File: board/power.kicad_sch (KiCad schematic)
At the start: 10 parts, among them U2 OKI

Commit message: Fan, Light, Buck
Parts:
- removed R1: 1.5k, Resistor_SMD:R_0603_1608Metric_Pad0.98x0.95mm_HandSolder, symbol Device:R
- removed R2: 100, Resistor_SMD:R_0603_1608Metric_Pad0.98x0.95mm_HandSolder, symbol Device:R
- removed R3: 220, Resistor_SMD:R_0603_1608Metric_Pad0.98x0.95mm_HandSolder, symbol Device:R
- removed U2: OKI, MRDT_Devices:OKI_Horizontal, symbol MRDT_Devices:OKI
- added D19: Green, LED_SMD:LED_0603_1608Metric_Pad1.05x0.95mm_HandSolder, symbol Device:LED
- added R1: 820, symbol Device:R_US
- added R2: 6.8k, symbol Device:R_US
- added R23: 3k, symbol Device:R_US
- added R3: 330, symbol Device:R_US
- added U2: OKI-78SR-12_1.0-W36H-C, Converter_DCDC:Converter_DCDC_Murata_OKI-78SR_Horizontal, symbol Converter_DCDC:OKI-78SR-12_1.0-W36H-C
- added U3: SHHD003A0A, MRDT_Devices:SHHD003A0A41Z_Through_Hole, symbol MRDT_Devices:SHHD003A0A
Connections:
- net +3.3V: now also R3.1
- net +5V: now also R1.1, U3.6 (Vout+); no longer C2.1
- net GND: now also D19.1 (K), U2.2 (GND), U3.2 (Vin-), U3.3 (On/OFF), U3.4 (Vout-)
- net VCC: now also R2.1, U2.1 (IN), U3.1 (Vin+)
- net at D1.2 (A): now also R2.2
- net at D2.2 (A): now also R3.2
- net at D3.2 (A): now also R1.2
- new net: D19.2 (A), R23.2
- new net +12V: C2.1, R23.1, U2.3 (OUT)
- no-connect marks 0 -> 1
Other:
- moved on the sheet: D1, D2, D3

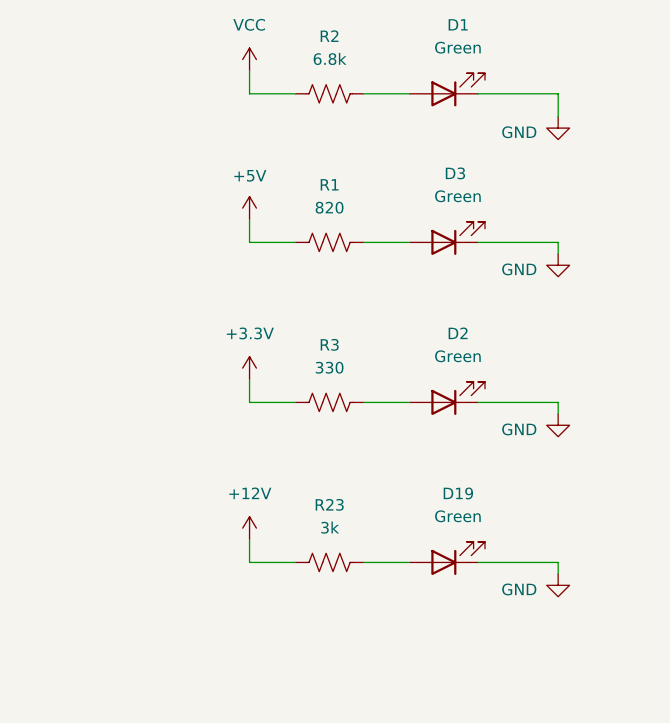
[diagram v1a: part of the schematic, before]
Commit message: Added most Footprints, Schematic review touch up
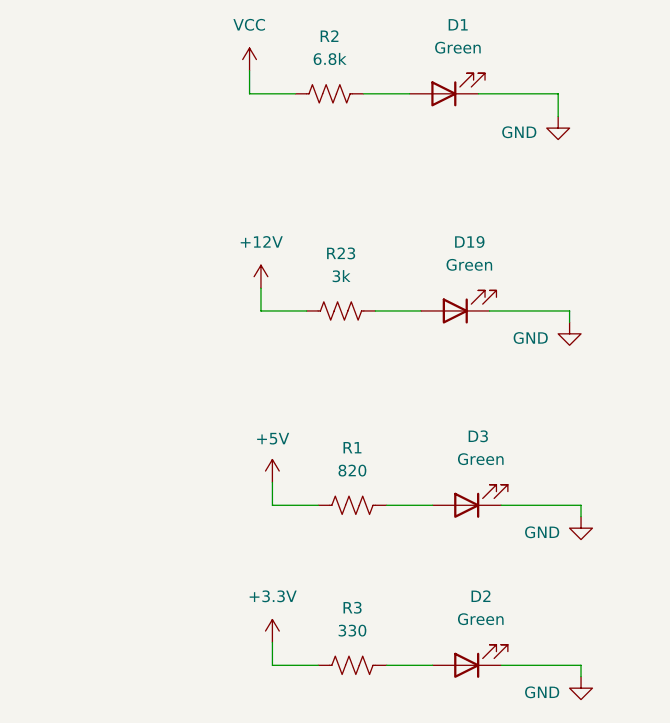
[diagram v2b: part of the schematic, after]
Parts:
- R1, R2, R23, R3: footprint (none) -> Resistor_SMD:R_0603_1608Metric_Pad0.98x0.95mm_HandSolder
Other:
- moved on the sheet: D19, D2, D3, R1, R23, R3

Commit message: Layout edits
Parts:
- removed Conn1: AndersonPP, MRDT_Connectors:Square_Anderson_2_H_Side_By_Side_PV, symbol MRDT_Connectors:AndersonPP
- added D20: MMSZ5240BT1G, MRDT_Devices:SOD-123_ONS-L, symbol MRDT_Devices:MMSZ5240BT1G
- added J2: 768250002, CoreBoard:CONN_SD-76825-0100_02_MOL, symbol CoreBoard:768250002
- added MOSFET1: TPC8132_LQS, MRDT_Devices:SOP-8_TOS-L, symbol MRDT_Devices:TPC8132_LQS
- added R10: 1k, Resistor_SMD:R_0603_1608Metric_Pad0.98x0.95mm_HandSolder, symbol Device:R_US
- U3: footprint MRDT_Devices:SHHD003A0A41Z_Through_Hole -> MRDT_Devices:SHHD003A0A-SRZ_Surface_Mount
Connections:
- net GND: now also D20.2, J2.1, R10.1
- new net: J2.2, MOSFET1.5 (DRAIN), MOSFET1.6 (DRAIN), MOSFET1.7 (DRAIN), MOSFET1.8 (DRAIN)
- new net: MOSFET1.4 (GATE), R10.2
- new net +24V: D20.1, MOSFET1.1 (SOURCE), MOSFET1.2 (SOURCE), MOSFET1.3 (SOURCE)

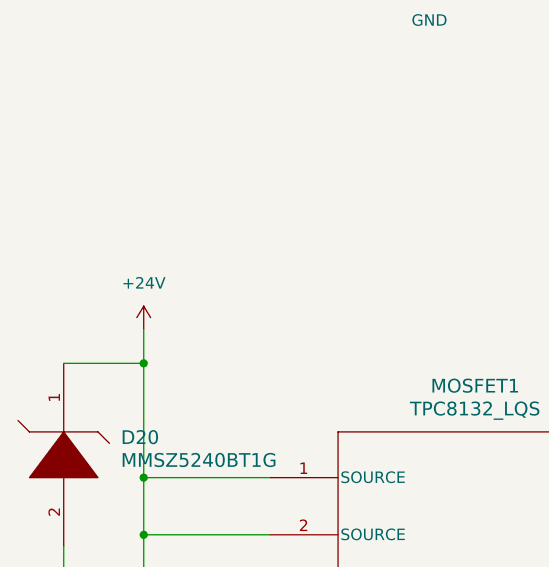
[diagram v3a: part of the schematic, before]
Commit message: routed core board
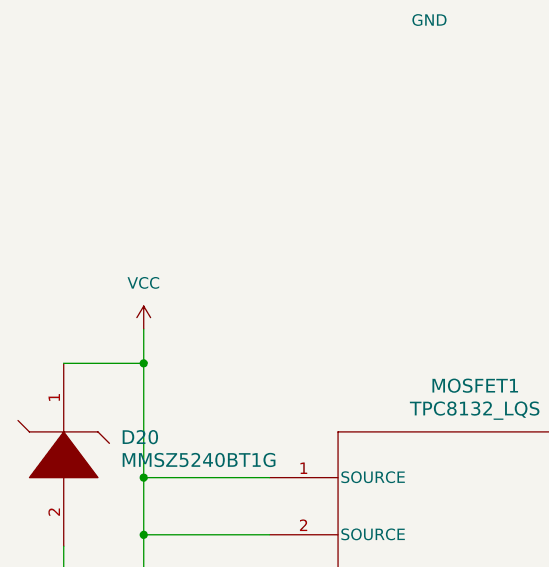
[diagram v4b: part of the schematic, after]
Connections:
- net +24V is gone; now on net VCC: D20.1, MOSFET1.1 (SOURCE), MOSFET1.2 (SOURCE), MOSFET1.3 (SOURCE)

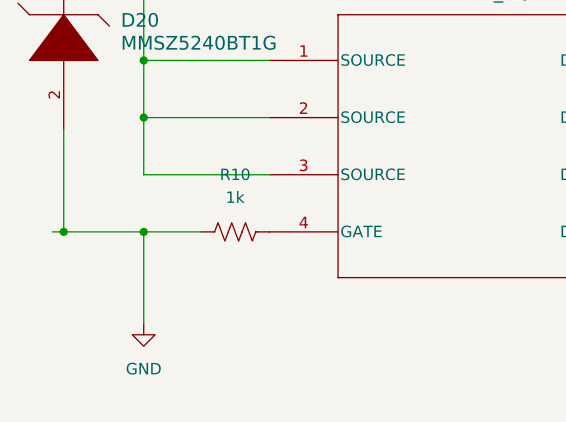
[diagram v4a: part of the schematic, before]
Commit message: Cleaned up traces and silkscreens
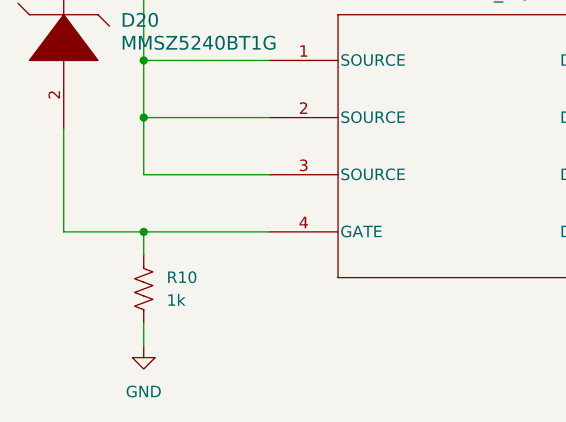
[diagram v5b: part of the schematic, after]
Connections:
- net GND: no longer D20.2
- net at MOSFET1.4 (GATE), R10.2: now also D20.2
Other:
- moved on the sheet: R10

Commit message: rev2 progress
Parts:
- removed U3: SHHD003A0A, MRDT_Devices:SHHD003A0A-SRZ_Surface_Mount, symbol MRDT_Devices:SHHD003A0A
- added C4: 10µF, Capacitor_SMD:C_1206_3216Metric_Pad1.33x1.80mm_HandSolder, symbol Device:C
- added C5: 10µF, Capacitor_SMD:C_0603_1608Metric_Pad1.08x0.95mm_HandSolder, symbol Device:C
- added U7: OKI-78SR-5_1.5-W36H-C, Converter_DCDC:Converter_DCDC_Murata_OKI-78SR_Horizontal, symbol Converter_DCDC:OKI-78SR-5_1.5-W36H-C
- MOSFET1: footprint MRDT_Devices:SOP-8_TOS-L -> CoreBoard:MSOP8_MC_MCH-L
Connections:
- net +12V: now also C5.1, U7.3 (OUT)
- net GND: now also C4.2, C5.2, U7.2 (GND)
- net VCC: now also C4.1, U7.1 (IN)
- no-connect marks 1 -> 0

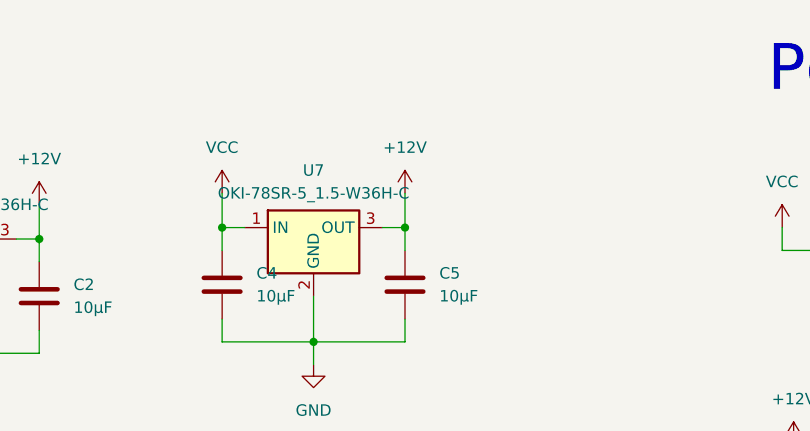
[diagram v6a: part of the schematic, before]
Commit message: move things for buck circuit
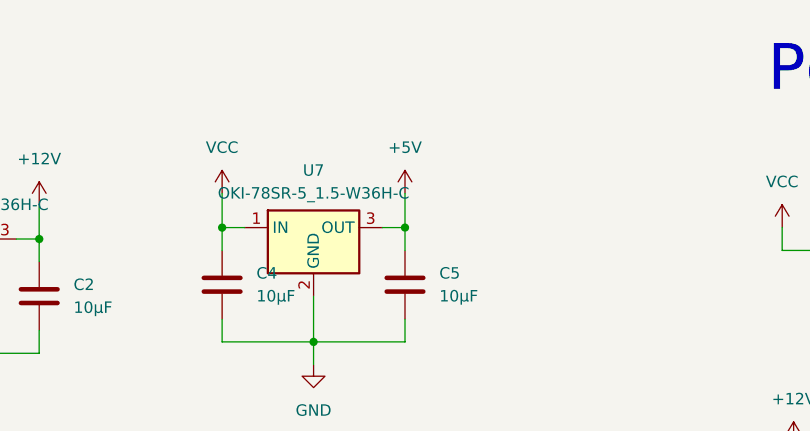
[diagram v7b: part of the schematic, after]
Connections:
- net +12V: no longer C5.1, U7.3 (OUT)
- net +5V: now also C5.1, U7.3 (OUT)

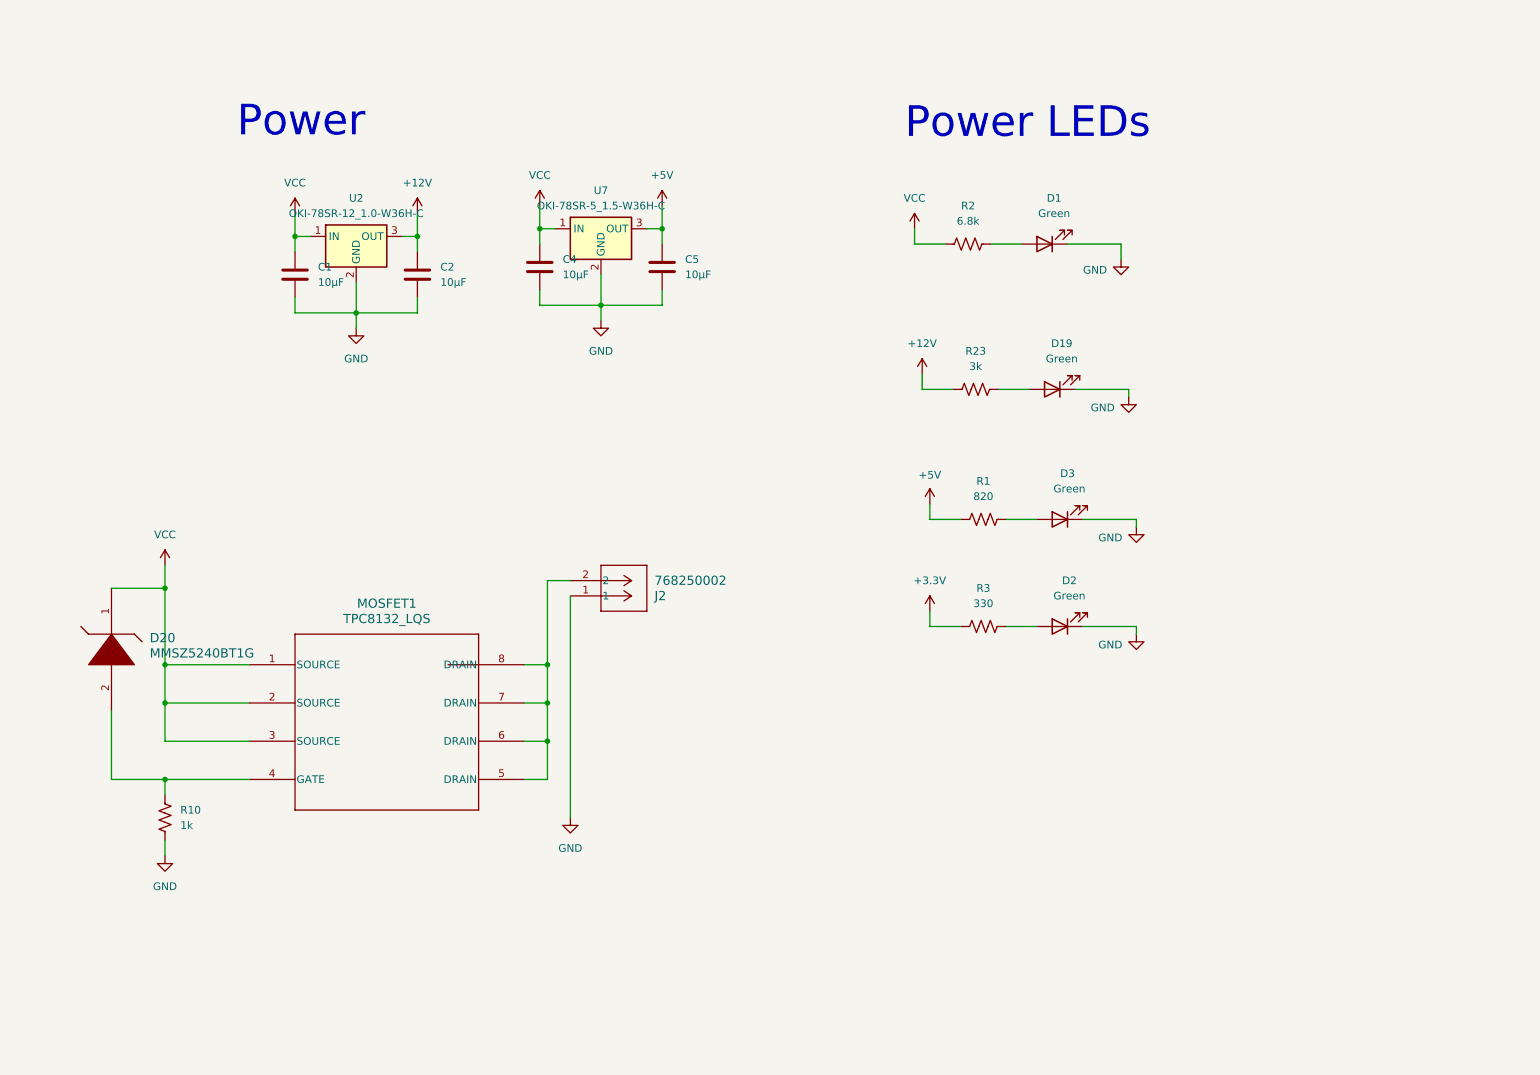
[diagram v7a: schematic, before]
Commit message: Add plated mounting holes and buck converter
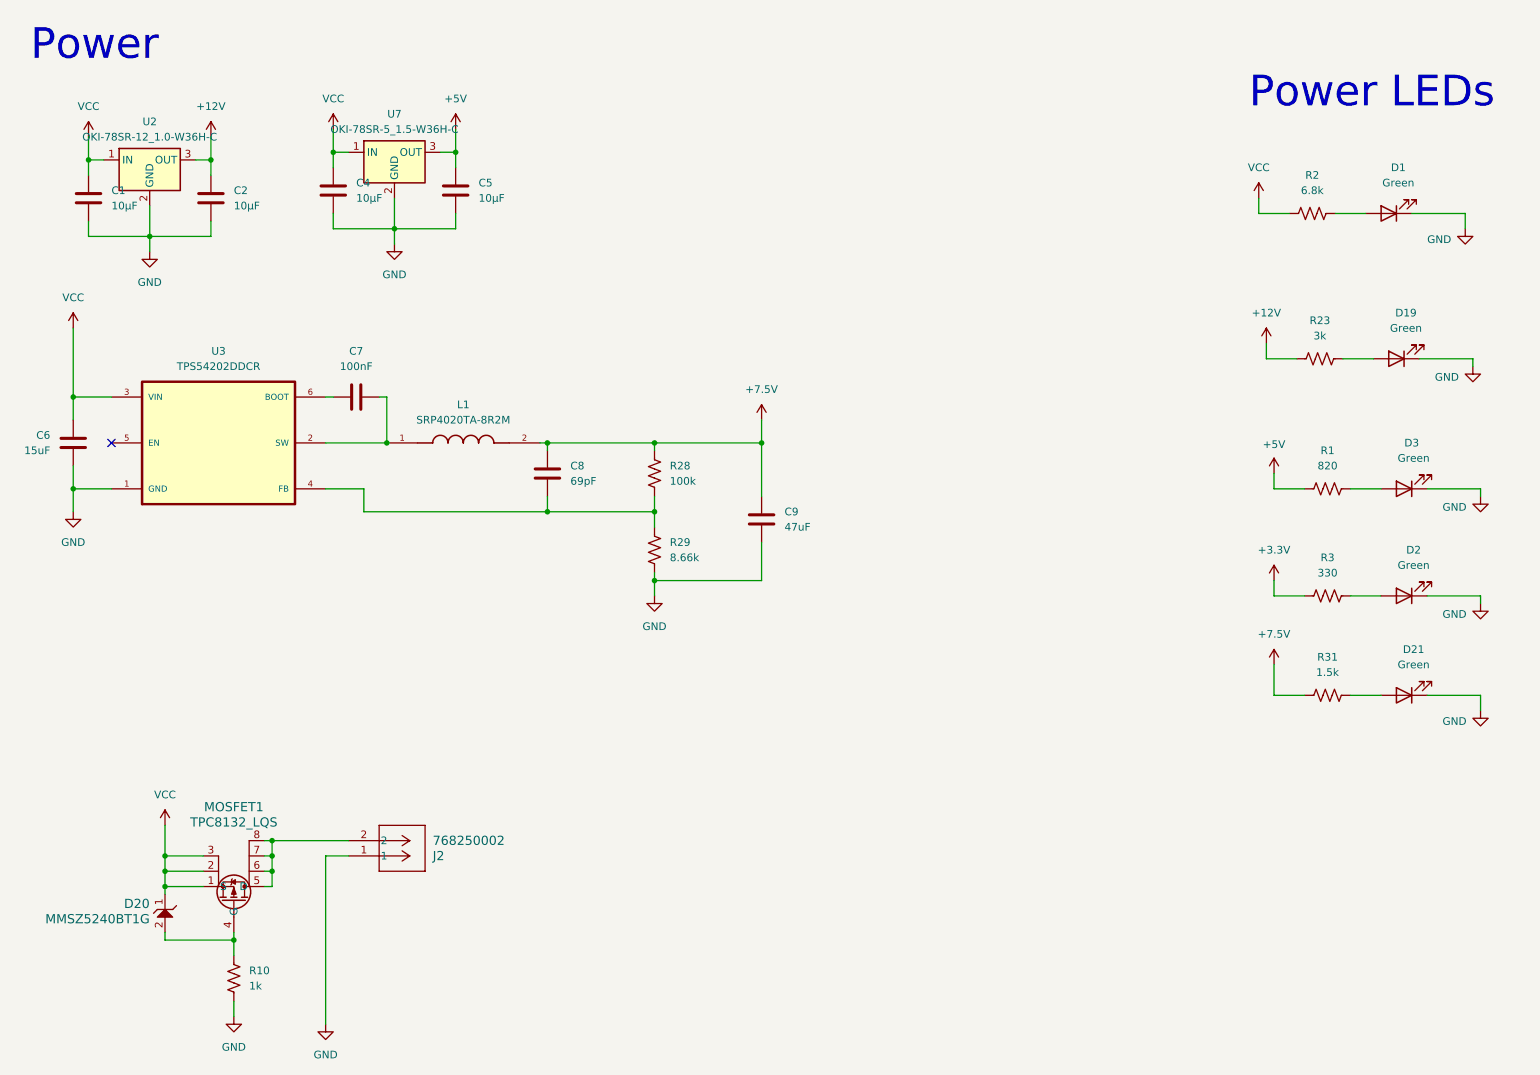
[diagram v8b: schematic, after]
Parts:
- added C6: 15uF, Capacitor_SMD:C_0805_2012Metric_Pad1.18x1.45mm_HandSolder, symbol Device:C
- added C7: 100nF, Capacitor_SMD:C_0603_1608Metric, symbol Device:C
- added C8: 69pF, Capacitor_SMD:C_0603_1608Metric, symbol Device:C
- added C9: 47uF, Capacitor_SMD:C_1206_3216Metric, symbol Device:C
- added D21: Green, LED_SMD:LED_0603_1608Metric_Pad1.05x0.95mm_HandSolder, symbol Device:LED
- added L1: SRP4020TA-8R2M, CoreBoard:IND_SRP4020TA-8R2M, symbol CoreBoard:SRP4020TA-8R2M
- added R28: 100k, Resistor_SMD:R_0603_1608Metric, symbol Device:R_US
- added R29: 8.66k, Resistor_SMD:R_0603_1608Metric, symbol Device:R_US
- added R31: 1.5k, Resistor_SMD:R_0603_1608Metric_Pad0.98x0.95mm_HandSolder, symbol Device:R_US
- added U3: TPS54202DDCR, CoreBoard:SOT95P280X110-6N, symbol CoreBoard:TPS54202DDCR
- J2: footprint CoreBoard:CONN_SD-76825-0100_02_MOL -> MRDT_Connectors:MOLEX_MegaFit_02_Horizontal; symbol CoreBoard:768250002 -> MRDT_Connectors:Molex_Megafit_02
- MOSFET1: footprint CoreBoard:MSOP8_MC_MCH-L -> Package_SO:SOIC-8_3.9x4.9mm_P1.27mm
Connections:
- net GND: now also C6.2, C9.2, D21.1 (K), R29.2, U3.1 (GND)
- net VCC: now also C6.1, U3.3 (VIN)
- new net: C7.2, L1.1, U3.2 (SW)
- new net: C8.2, R28.2, R29.1, U3.4 (FB)
- new net: C7.1, U3.6 (BOOT)
- new net: D21.2 (A), R31.2
- new net +7.5V: C8.1, C9.1, L1.2, R28.1, R31.1
- no-connect marks 0 -> 1
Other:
- moved on the sheet: C1, C2, C4, C5, D1, D19, D2, D20, D3, J2, R1, R10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
